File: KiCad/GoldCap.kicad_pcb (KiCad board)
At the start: 2 copper layers, 38.1 x 48.9 mm, 46 parts, among them J1 Pwr In, J2 Pwr Out, J3 Prog Jumper, J4 Prog, J5 Conn_01x09_Male, J6 Main Pwr, Q1 BC847, Q2 IRLML6401, SW1 SW_TACTILE_SPST, U1 TPS70933DBV, U2 ATtiny20-SSU

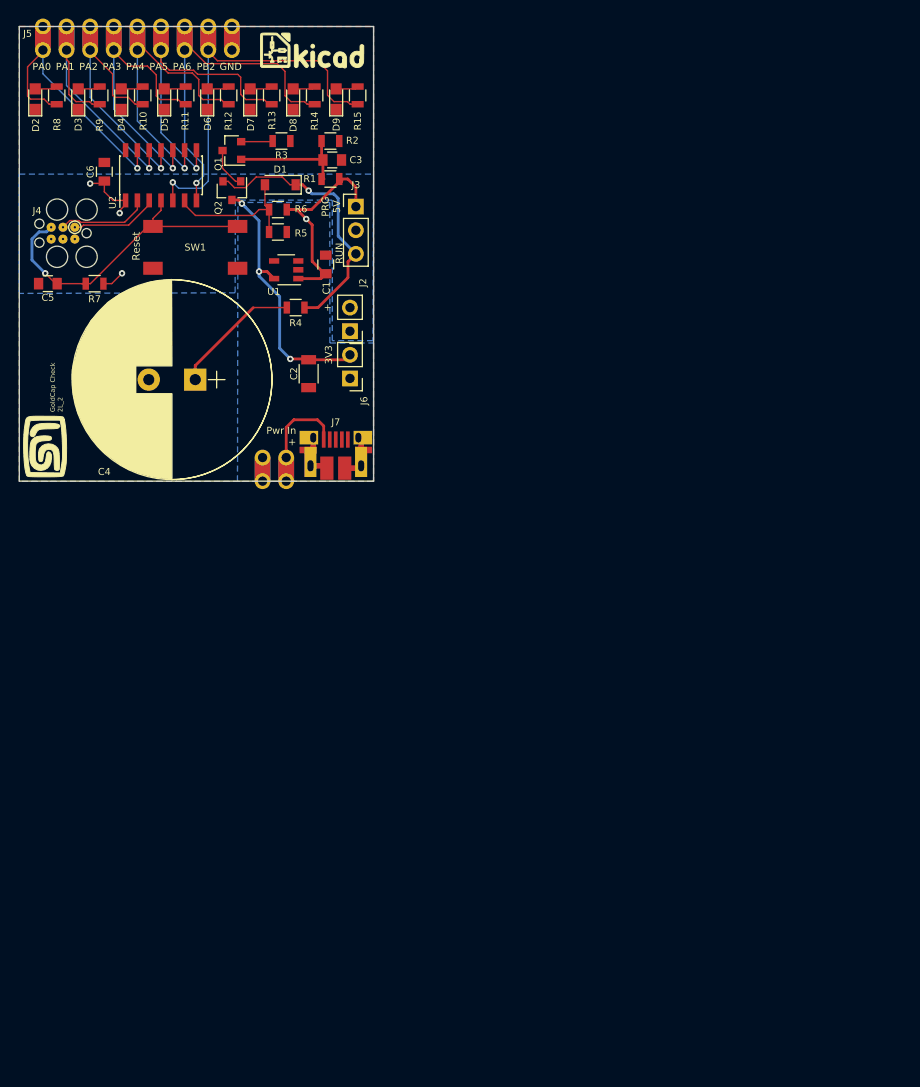
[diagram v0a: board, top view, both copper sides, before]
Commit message: Revision 3 of the board plus new 3D elements
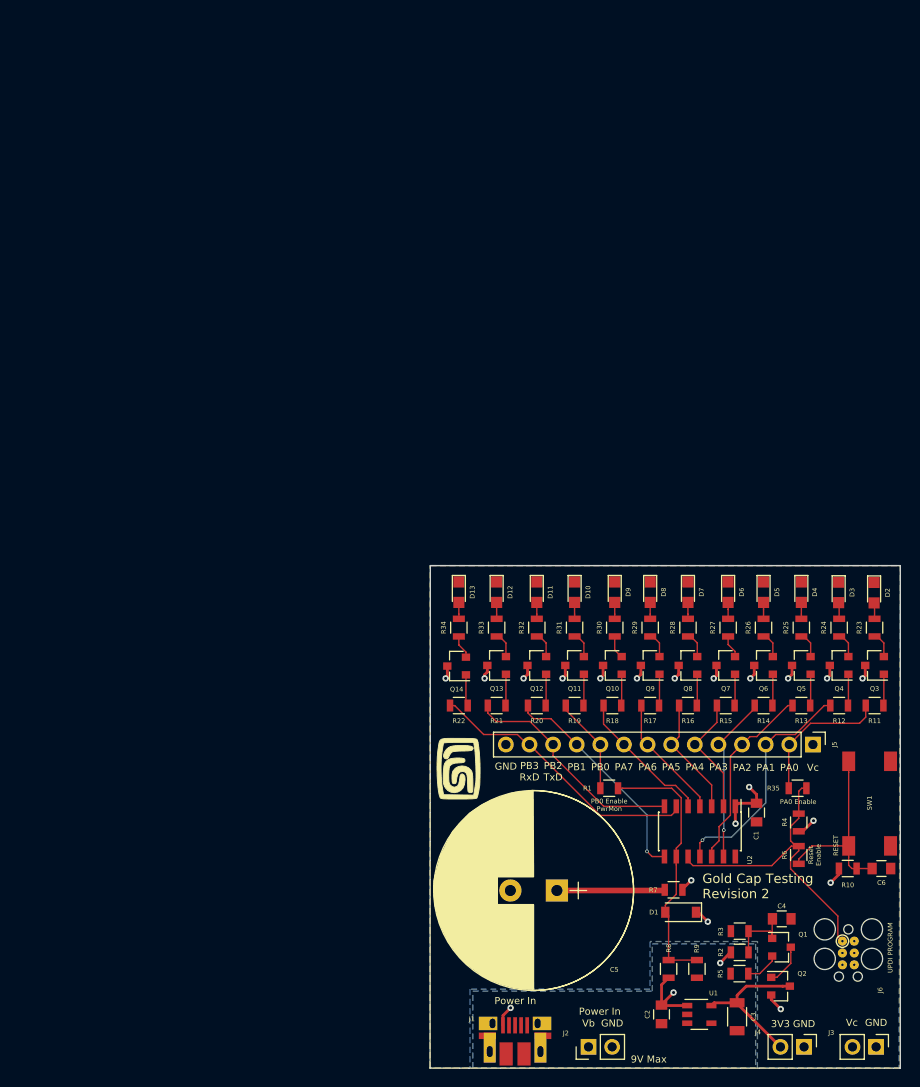
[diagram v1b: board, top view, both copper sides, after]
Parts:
- removed ?: , GoldCap-Check:KiCad-Logo
- removed the G*** at (73.9, 56.6)
- removed J7: ~, GoldCap-Check:USB_B_2.0_Micro
- removed LG: LG, GoldCap-Check:MyBasic_rounded_50_1
- removed REF***: KiCad-Logo2_6mm_SilkScreen, Symbols:KiCad-Logo2_6mm_SilkScreen
- added D10: LED, LEDs:LED_0805, F.Cu at (110.5, 88.8)
- added D11: LED, LEDs:LED_0805, F.Cu at (106.5, 88.8)
- added D12: LED, LEDs:LED_0805, F.Cu at (102.1, 88.8)
- added D13: LED, LEDs:LED_0805, F.Cu at (98.1, 88.8)
- added G***: LOGO, GoldCap-Check:MyBasic_rounded_50_1, F.Cu at (98.0, 107.8)
- added G***: LOGO, GoldCap-Check:MyBasic_rounded_50_1, B.Cu at (141.3, 89.9)
- added G***: LOGO, GoldCap-Check:KiCad-Logo, B.Cu at (101.1, 89.9)
- added Q10: BC847, TO_SOT_Packages_SMD:SOT-23, F.Cu at (114.6, 96.6)
- added Q11: BC847, TO_SOT_Packages_SMD:SOT-23, F.Cu at (110.5, 96.6)
- added Q12: BC847, TO_SOT_Packages_SMD:SOT-23, F.Cu at (106.5, 96.6)
- added Q13: BC847, TO_SOT_Packages_SMD:SOT-23, F.Cu at (102.1, 96.6)
- added Q14: BC847, TO_SOT_Packages_SMD:SOT-23, F.Cu at (97.8, 96.7)
- added Q3: BC847, TO_SOT_Packages_SMD:SOT-23, F.Cu at (142.8, 96.6)
- added Q4: BC847, TO_SOT_Packages_SMD:SOT-23, F.Cu at (139.0, 96.6)
- added Q5: BC847, TO_SOT_Packages_SMD:SOT-23, F.Cu at (134.9, 96.6)
- added Q6: BC847, TO_SOT_Packages_SMD:SOT-23, F.Cu at (130.8, 96.6)
- added Q7: BC847, TO_SOT_Packages_SMD:SOT-23, F.Cu at (126.8, 96.6)
- added Q8: BC847, TO_SOT_Packages_SMD:SOT-23, F.Cu at (122.7, 96.6)
- added Q9: BC847, TO_SOT_Packages_SMD:SOT-23, F.Cu at (118.6, 96.6)
- added R16: 10kΩ, Resistors_SMD:R_0805, F.Cu at (122.7, 101.0)
- added R17: 10kΩ, Resistors_SMD:R_0805, F.Cu at (118.6, 101.0)
- added R18: 10kΩ, Resistors_SMD:R_0805, F.Cu at (114.6, 101.0)
- added R19: 10kΩ, Resistors_SMD:R_0805, F.Cu at (110.5, 101.0)
- added R20: 10kΩ, Resistors_SMD:R_0805, F.Cu at (106.5, 101.0)
- added R21: 10kΩ, Resistors_SMD:R_0805, F.Cu at (102.1, 101.0)
- added R22: 10kΩ, Resistors_SMD:R_0805, F.Cu at (98.1, 101.0)
- added R23: 100Ω, Resistors_SMD:R_0805, F.Cu at (142.8, 92.6)
- added R24: 100Ω, Resistors_SMD:R_0805, F.Cu at (139.0, 92.6)
- added R25: 100Ω, Resistors_SMD:R_0805, F.Cu at (134.9, 92.6)
- added R26: 100Ω, Resistors_SMD:R_0805, F.Cu at (130.8, 92.6)
- added R27: 100Ω, Resistors_SMD:R_0805, F.Cu at (127.0, 92.6)
- added R28: 100Ω, Resistors_SMD:R_0805, F.Cu at (122.7, 92.6)
- added R29: 100Ω, Resistors_SMD:R_0805, F.Cu at (118.6, 92.6)
- added R30: 100Ω, Resistors_SMD:R_0805, F.Cu at (114.8, 92.6)
- added R31: 100Ω, Resistors_SMD:R_0805, F.Cu at (110.5, 92.6)
- added R32: 100Ω, Resistors_SMD:R_0805, F.Cu at (106.5, 92.6)
- added R33: 100Ω, Resistors_SMD:R_0805, F.Cu at (102.1, 92.6)
- added R34: 100Ω, Resistors_SMD:R_0805, F.Cu at (98.1, 92.6)
- added R35: 0Ω, Resistors_SMD:R_0805, F.Cu at (134.5, 109.9)
- C1: value 1μF -> 100n
- C2: value 2.2μF -> 1μF; footprint Capacitors_SMD:C_1206 -> Capacitors_SMD:C_0805
- C3: value 100n -> 2.2μF; footprint Capacitors_SMD:C_0805 -> Capacitors_SMD:C_1206
- C4: value 470m 5V5 -> 100n; footprint GoldCap-Check:CP_Radial_D21.5mm_P5.00mm -> Capacitors_SMD:C_0805
- C5: value 100n -> 470m 5V5; footprint Capacitors_SMD:C_0805 -> GoldCap-Check:CP_Radial_D21.5mm_P5.00mm
- J1: value Pwr In -> ~; footprint GoldCap-Check:Castillation_2_2.54 -> GoldCap-Check:USB_B_2.0_Micro
- J2: value Pwr Out -> Pwr In
- J3: value Prog Jumper -> Pwr Out; footprint Pin_Headers:Pin_Header_Straight_1x03_Pitch2.54mm -> Pin_Headers:Pin_Header_Straight_1x02_Pitch2.54mm
- J4: value Prog -> Main Pwr; footprint GoldCap-Check:PRG_TC2030-IDC-FP_TH -> Pin_Headers:Pin_Header_Straight_1x02_Pitch2.54mm
- J5: value Conn_01x09_Male -> Conn_01x14_Male; footprint GoldCap-Check:Castillation_9_2.54 -> Pin_Headers:Pin_Header_Straight_1x14_Pitch2.54mm
- J6: value Main Pwr -> Prog; footprint Pin_Headers:Pin_Header_Straight_1x02_Pitch2.54mm -> GoldCap-Check:PRG_TC2030-IDC-FP_TH
- R1: value 100k -> 0Ω
- R10: value 260k -> 10k
- R11, R12, R13, R14, R15: value 260k -> 10kΩ
- R2: value 10k -> 100k
- R3: value 100 -> 10k
- R4: value 33 -> 47kΩ
- R5: value 68k -> 100
- R6: value 27k -> 0Ω
- R7: value 10k -> 33
- R8: value 260k -> 68k
- R9: value 260k -> 27k
- U2: value ATtiny20-SSU -> ATtiny1614-SS
- moved J4 118.0 mm to (135.2, 137.7), turned to 270 degrees
- moved R8 114.7 mm to (120.6, 129.3)
- moved R9 113.8 mm to (123.7, 129.3), turned to 270 degrees
- moved R10 112.5 mm to (139.9, 118.5), turned to 0 degrees
- moved C6 112.2 mm to (143.5, 118.5), turned to 0 degrees
- moved J5 111.5 mm to (136.1, 105.2), turned to 270 degrees
- moved J3 106.3 mm to (142.9, 137.7), turned to 270 degrees
- moved D2 104.7 mm to (142.7, 88.8), turned to 270 degrees
- moved Q1 104.1 mm to (132.8, 126.9), turned to 0 degrees
- moved Q2 103.9 mm to (132.7, 131.1), turned to 0 degrees
- moved C3 101.9 mm to (128.0, 134.4), turned to 270 degrees
- moved R11 99.0 mm to (142.8, 101.0), turned to 180 degrees
- moved R3 98.2 mm to (128.3, 125.2), turned to 180 degrees
- moved R2 97.7 mm to (128.3, 127.5), turned to 180 degrees
- moved D3 97.5 mm to (138.9, 88.8), turned to 270 degrees
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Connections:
- C1 pad 1: /Vb -> /Vc
- C2 pad 1: /3V3 -> /Vb
- C3 pad 1: Net-(C3-Pad1) -> /3V3
- C5 pad 1: /~RESET -> Net-(C5-Pad1)
- C6 pad 1: /Vc -> /~RESET
- D1 pad 1: /Vg -> /Vc
- J1 pad 2: GND -> Net-(J1-Pad2)
- J2 pad 1: GND -> /Vb
- J2 pad 2: /Vc -> GND
- J3 pad 1: /Vb -> GND
- J4 pad 1: /TPIDATA -> GND
- J4 pad 2: /Vc -> /3V3
- J5 pad 1: /LED_PA0 -> /Vc
- J5 pad 2: /LED_PA1 -> /LED_PA0
- J5 pad 3: /LED_PA2 -> /LED_PA1
- J5 pad 4: /LED_PA3 -> /LED_PA2
- J5 pad 5: /LED_PA4 -> /LED_PA3
- J5 pad 6: /LED_PA5 -> /LED_PA4
- J5 pad 7: /LED_PA6 -> /LED_PA5
- J5 pad 8: /LED_PB2 -> /LED_PA6
- J5 pad 9: GND -> /LED_PA7
- J6 pad 1: GND -> /PDI_DATA
- J6 pad 2: /3V3 -> /Vc
- Q1 pad 1: Net-(C3-Pad1) -> Net-(C4-Pad1)
- Q2 pad 2: /Vg -> /Vc
- R1 pad 1: Net-(C3-Pad1) -> /PwrMon
- R1 pad 2: /Vb -> /LED_PB0
- R10 pad 1: /LED_PA2 -> /Vc
- R10 pad 2: Net-(D4-Pad2) -> /~RESET
- R11 pad 1: /LED_PA3 -> Net-(Q3-Pad1)
- R11 pad 2: Net-(D5-Pad2) -> /LED_PA0
- R12 pad 1: /LED_PA4 -> Net-(Q4-Pad1)
- R12 pad 2: Net-(D6-Pad2) -> /LED_PA1
- R13 pad 1: /LED_PA5 -> Net-(Q5-Pad1)
- R13 pad 2: Net-(D7-Pad2) -> /LED_PA2
- R14 pad 1: /LED_PA6 -> Net-(Q6-Pad1)
- R14 pad 2: Net-(D8-Pad2) -> /LED_PA3
- R15 pad 1: /LED_PB2 -> Net-(Q7-Pad1)
- R15 pad 2: Net-(D9-Pad2) -> /LED_PA4
- R2 pad 1: Net-(C3-Pad1) -> Net-(C4-Pad1)
- R2 pad 2: GND -> /Vb
- R3 pad 1: Net-(Q1-Pad2) -> Net-(C4-Pad1)
- R4 pad 1: /Vg -> /Vc
- R4 pad 2: Net-(C4-Pad1) -> /PDI_DATA
- R5 pad 1: /Vb -> Net-(Q1-Pad2)
- R5 pad 2: /PwrMon -> GND
- R6 pad 1: /PwrMon -> /~RESET
- R6 pad 2: GND -> /PDI_DATA
- R7 pad 2: /~RESET -> Net-(C5-Pad1)
- R8 pad 1: /LED_PA0 -> /Vb
- R8 pad 2: Net-(D2-Pad2) -> /PwrMon
- R9 pad 1: /LED_PA1 -> /PwrMon
- R9 pad 2: Net-(D3-Pad2) -> GND
- U2 pad 10: /LED_PA3 -> /PDI_DATA
- U2 pad 11: /LED_PA2 -> /LED_PA1
- U2 pad 12: /LED_PA1 -> /LED_PA2
- U2 pad 13: /LED_PA0 -> /LED_PA3
- U2 pad 2: /TPICLK -> /LED_PA4
- U2 pad 3: /TPIDATA -> /LED_PA5
- U2 pad 4: /~RESET -> /LED_PA6
- U2 pad 5: /LED_PB2 -> /LED_PA7
- U2 pad 6: /PwrMon -> /LED_PB3_RxD
- U2 pad 7: /LED_PA6 -> /LED_PB2_TxD
- U2 pad 8: /LED_PA5 -> /LED_PB1
- U2 pad 9: /LED_PA4 -> /PwrMon
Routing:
- net /LED_PB2: track 43.5 -> 0.00 mm, vias 1 -> 0
- net /PDI_DATA: track 0.00 -> 34.1 mm
- net /LED_PB3_RxD: track 0.00 -> 29.9 mm
- net /Vg: track 29.8 -> 0.00 mm, vias 1 -> 0
- net /LED_PB2_TxD: track 0.00 -> 24.7 mm
- net /Vc: track 9.20 -> 33.7 mm, vias 3 -> 19
- net /LED_PA5: track 37.3 -> 13.0 mm, vias 1 -> 0
- net /LED_PB1: track 0.00 -> 24.2 mm, vias 0 -> 1
- net /LED_PA6: track 37.3 -> 13.4 mm, vias 1 -> 0
- net /Vb: track 34.9 -> 11.8 mm, vias 1 -> 3
- net /LED_PA4: track 34.0 -> 13.1 mm, vias 1 -> 0
- net /LED_PA7: track 0.00 -> 15.3 mm
- net /LED_PA0: track 30.5 -> 15.4 mm, vias 1 -> 0
- net /~RESET: track 33.8 -> 20.3 mm, vias 1 -> 0
- net Net-(C3-Pad1): track 13.2 -> 0.00 mm
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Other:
- board size 38.1 x 48.9 mm -> 50.6 x 54 mm
- net class Default: via_dia 0.6858 -> 0.381; via_drill 0.3302 -> 0.254
- net class Pwr added: clearance 0.1524, trace_width 0.3048, via_dia 0.6858, via_drill 0.3302
- rule via_min_drill: 0.3302 -> 0.254
- rule via_min_size: 0.6858 -> 0.381
- board text added: "9V Max"
- board text added: "Gold Cap Testing Revision 2"
- board text added: "PA0 Enable"
- board text added: "PA7"
- board text added: "PB0"
- board text added: "PB0 Enable PwrMon"
- board text added: "PB1"
- board text added: "PB2 TxD"
- board text added: "PB3 RxD"
- board text added: "Power In"
- board text added: "RESET"
- board text added: "Reset Enable"
- board text added: "UPDI PROGRAM"
- board text added: "Vb"
- board text added: "Vc"
- board text removed: "+"
- board text removed: "GoldCap Check 2L_2"
- board text removed: "In Programming Mode, do not exceed 5V"
- board text removed: "PA0 PA1 PA2 PA3 PA4 PA5 PA6 PB2 GND"
- board text removed: "PB2"
- board text removed: "PRG 5V"
- board text removed: "Pwr IN +"
- board text removed: "Pwr In +"
- board text removed: "RUN"
- board text removed: "Reset"

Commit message: Revision 3 final for OSHParch
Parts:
- removed the G*** at (98.0, 107.8)
- added J7: Main Pwr, Pin_Headers:Pin_Header_Straight_1x02_Pitch2.54mm, F.Cu at (97.5, 135.0)
- moved R7 25.9 mm to (97.5, 131.3), turned to 90 degrees
- moved J1 2.42 mm to (106.5, 137.8)
- moved J2 1.93 mm to (113.9, 137.7)
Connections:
- R7 pad 1: /Vc -> Net-(J7-Pad1)
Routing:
- net Net-(C5-Pad1): track 11.6 -> 16.1 mm
- net Net-(J7-Pad1): track 0.00 -> 2.76 mm
- net /Vc: track 33.7 -> 32.3 mm, vias 19 -> 18
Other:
- board text added: "GoldCap Enable"
- board text added: "PB2"
- board text added: "PB3"
- board text added: "RxD"
- board text added: "TxD"
